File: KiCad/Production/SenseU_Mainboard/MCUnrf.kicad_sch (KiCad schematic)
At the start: 5 parts

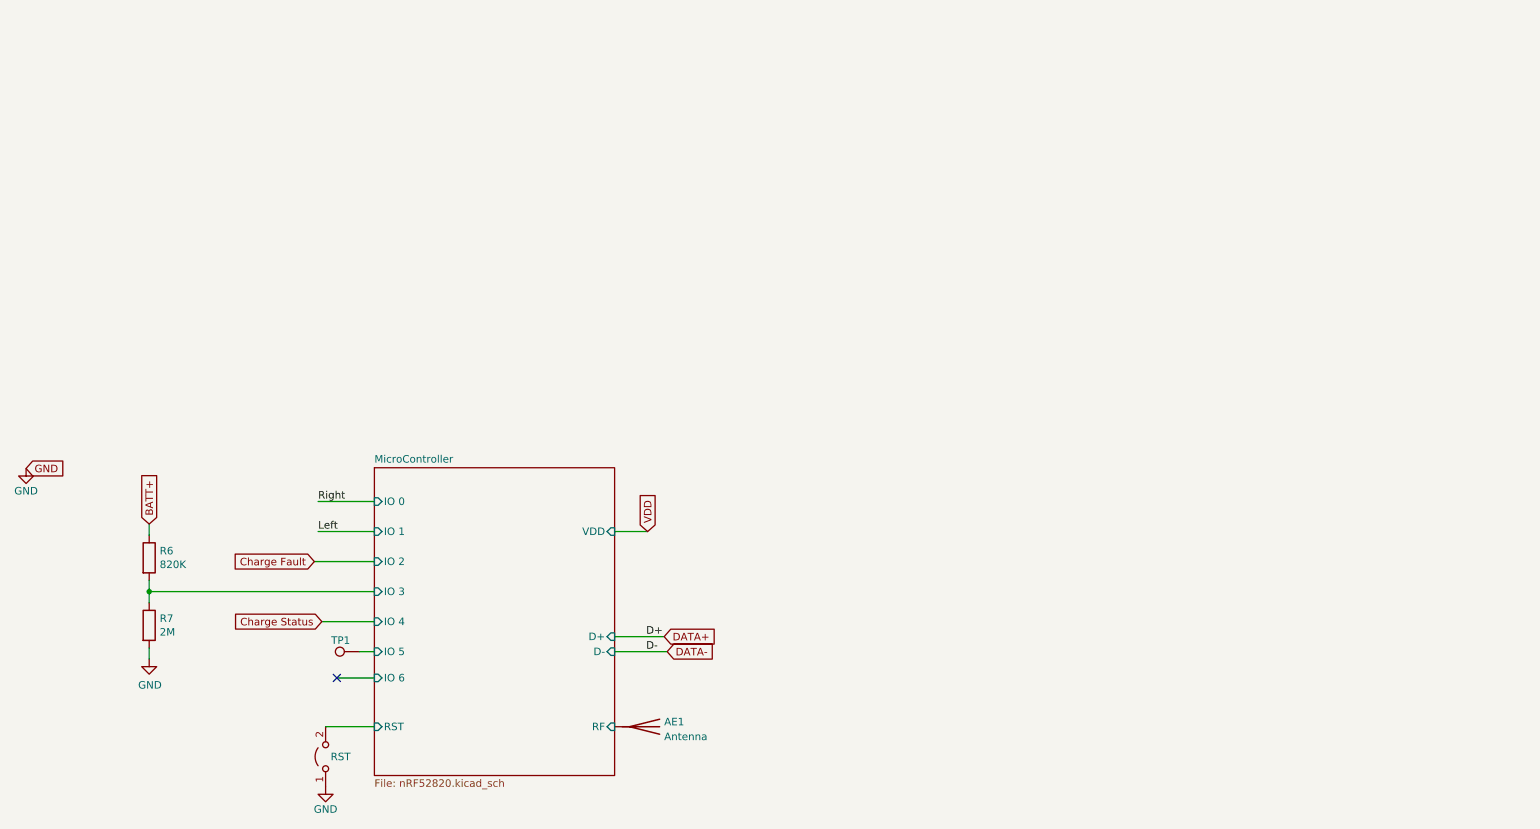
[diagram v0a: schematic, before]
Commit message: added fpga pins
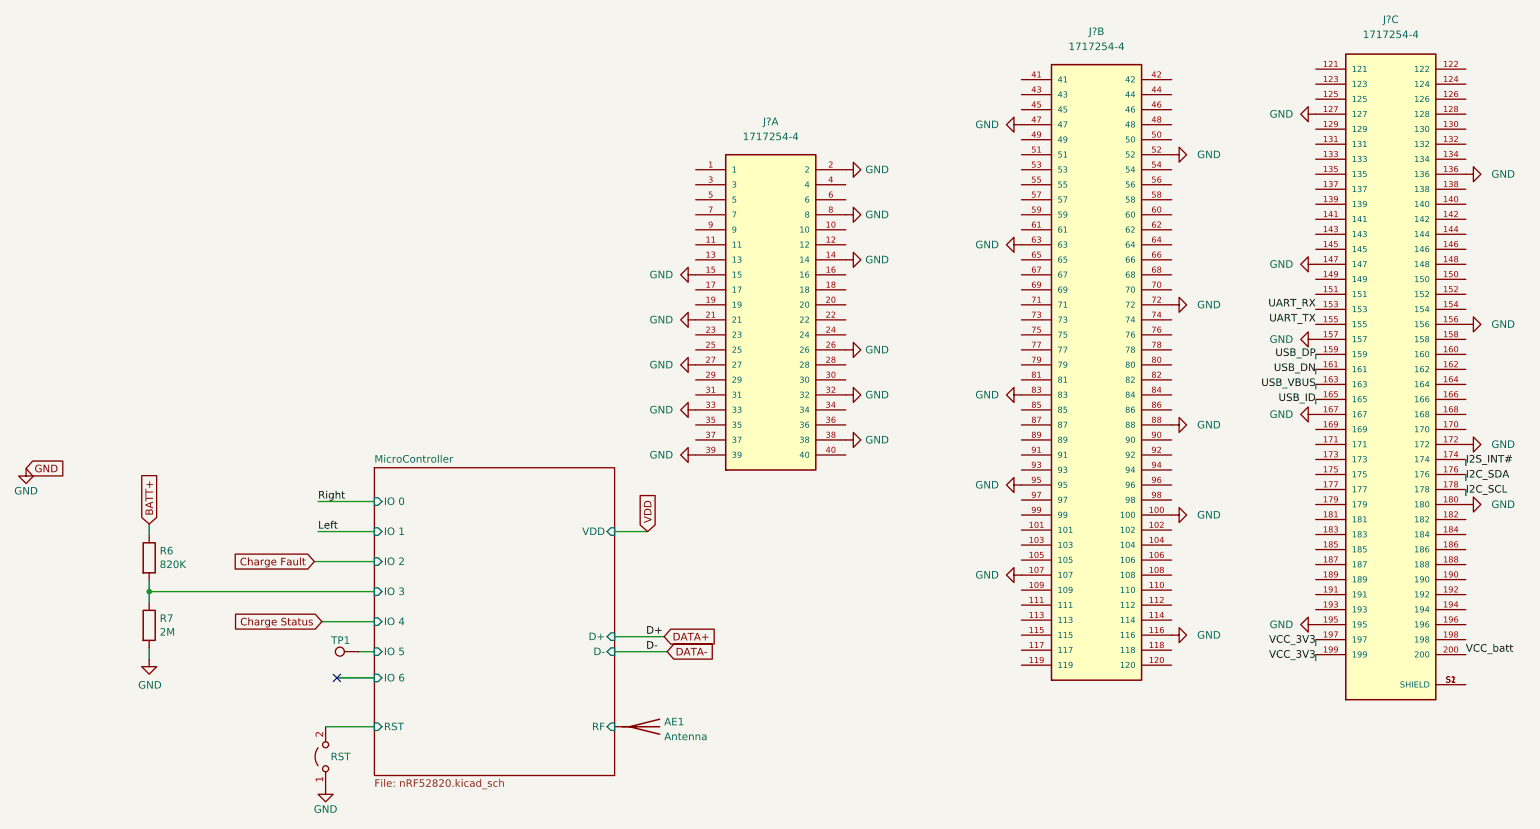
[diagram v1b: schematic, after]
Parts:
- added J? (x3): 1717254-4, TE_1717254-4, symbol 1717254-4:1717254-4
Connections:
- net GND: now also J?.100, J?.107, J?.116, J?.127, J?.136, J?.14, J?.147, J?.15, J?.156, J?.157, J?.167, J?.172, J?.180, J?.195, J?.2, J?.21, J?.26, J?.27, J?.32, J?.33, J?.38, J?.39, J?.47, J?.52, J?.63, J?.72, J?.8, J?.83, J?.88, J?.95
- new net: J?.S1 (SHIELD), J?.S2 (SHIELD)
- new net I2C_SCL: J?.178
- new net I2C_SDA: J?.176
- new net I2S_INT#: J?.174
- new net UART_RX: J?.153
- new net UART_TX: J?.155
- new net USB_DN: J?.161
- new net USB_DP: J?.159
- new net USB_ID: J?.165
- new net USB_VBUS: J?.163
- new net VCC_3V3: J?.197, J?.199
- new net VCC_batt: J?.200

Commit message: added a lot
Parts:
- removed J? (x3): 1717254-4, TE_1717254-4, symbol 1717254-4:1717254-4
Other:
- added sheet FPGA (FPGA.kicad_sch)
- added sheet Pmod (Pmod_connection.kicad_sch)
